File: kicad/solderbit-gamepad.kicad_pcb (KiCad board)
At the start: 2 copper layers, 114 x 49.3 mm, 46 parts, among them J1 Microbit_Edge_Connector, J2 S2B-PH-SM4-TB(LF)(SN), Q1 DMG2045U, SW1 MST22D18G2 125, U1 74HC165D,653, U2 NCP114ASN330T1G

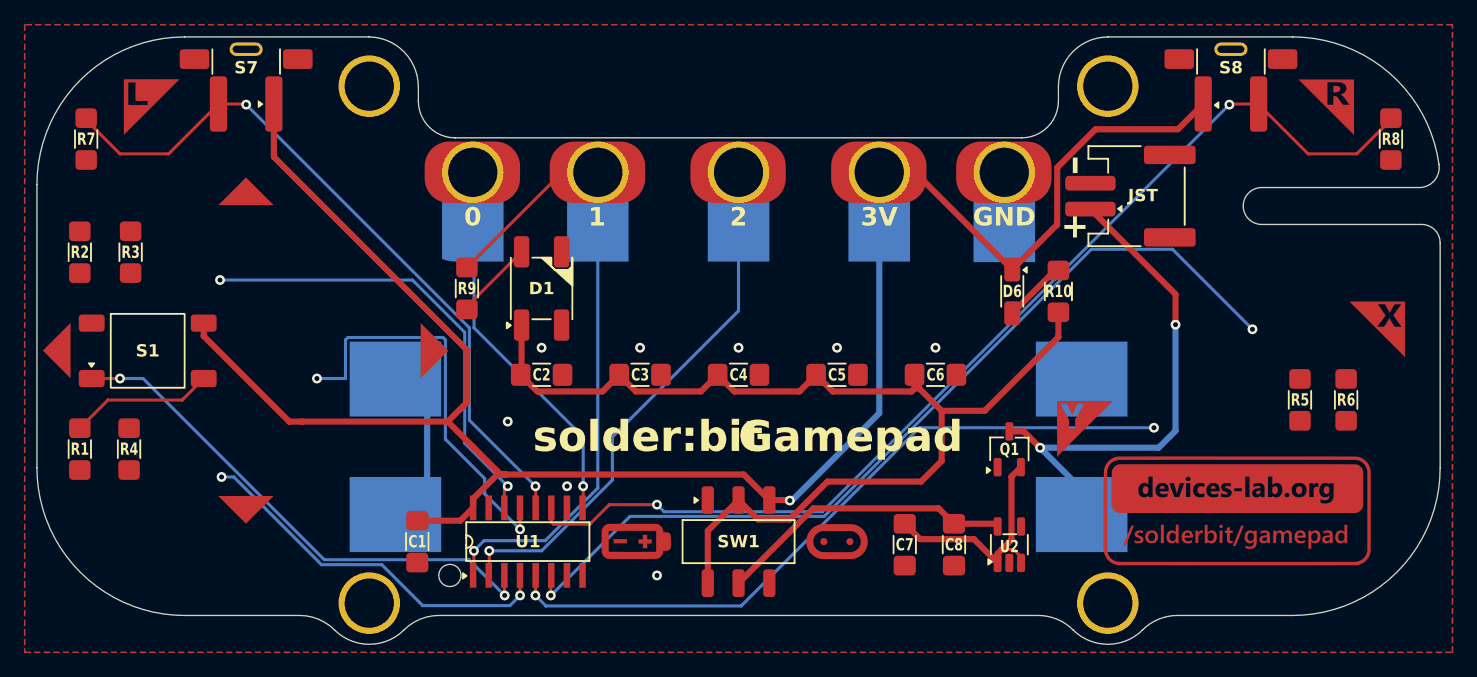
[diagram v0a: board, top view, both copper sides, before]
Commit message: Replace all with v0.9 and new media
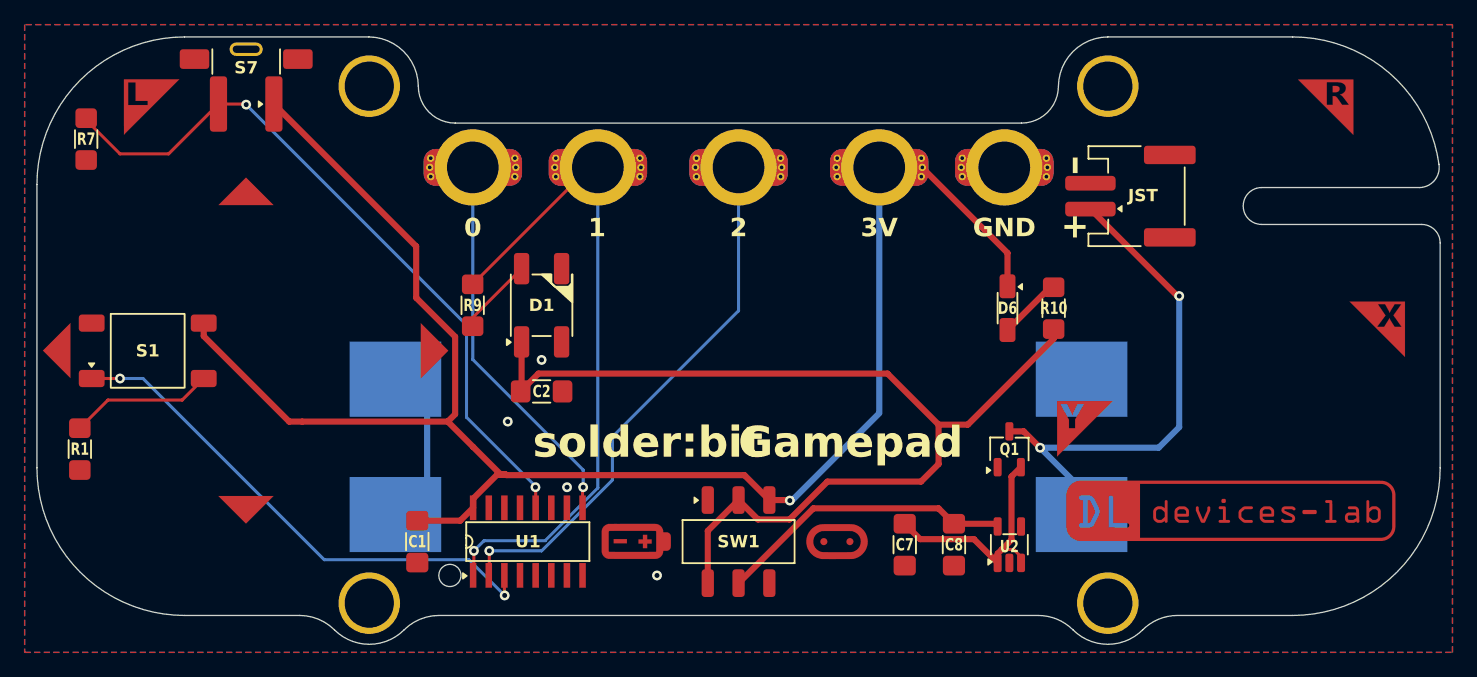
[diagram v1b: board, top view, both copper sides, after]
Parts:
- removed C3, C4, C5, C6: 1uF, Solderbit_Gamepad:1206_Capacitor
- removed G1: ~, Solderbit_Gamepad:Devices-Lab_Logo_H9mm
- removed G4: ~, Solderbit_Gamepad:UKRI_Logo
- removed J1: Microbit_Edge_Connector, Solderbit_Gamepad:Microbit_Edge_Connector
- removed R2, R3, R4, R5, R6, R8: 100k, Solderbit_Gamepad:1206_Resistor
- removed the Ref** at (62.2, 46.6)
- removed S8: TS-1037-A4B3-D2, Solderbit_Gamepad:Tactile_Switch_Right_90_Degrees
- added CN1: SMTSOM310BTR, Solderbit_Gamepad:SMTSOM310BTR, F.Cu at (82.7, 47.2)
- added CN2: SMTSOM310BTR, Solderbit_Gamepad:SMTSOM310BTR, F.Cu at (92.8, 47.2)
- added CN3: SMTSOM310BTR, Solderbit_Gamepad:SMTSOM310BTR, F.Cu at (104.3, 47.2)
- added CN4: SMTSOM310BTR, Solderbit_Gamepad:SMTSOM310BTR, F.Cu at (115.7, 47.2)
- added CN5: SMTSOM310BTR, Solderbit_Gamepad:SMTSOM310BTR, F.Cu at (125.9, 47.2)
- added G***: LOGO, LOGO, F.Cu at (144.3, 75.1)
- added G***: LOGO, LOGO, B.Cu at (147.0, 71.7)
- moved R9 1.44 mm to (82.7, 58.4)
- moved D6 1.42 mm to (126.1, 58.6)
- moved R10 1.42 mm to (129.9, 58.6)
- moved D1 1.36 mm to (88.3, 58.4)
- moved C2 1.35 mm to (88.3, 65.4)
- moved Ref** 0.05 mm to (152.0, 42.3)
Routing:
- net BTN_R_BUMP: track 87.0 -> 0.00 mm, vias 2 -> 0
- net BTN_X: track 73.0 -> 0.00 mm, vias 2 -> 0
- net BTN_Y: track 58.2 -> 0.00 mm, vias 2 -> 0
- net BTN_UP: track 37.5 -> 0.00 mm, vias 2 -> 0
- net BTN_RIGHT: track 33.4 -> 0.00 mm, vias 2 -> 0
- net BTN_DOWN: track 30.6 -> 0.00 mm, vias 2 -> 0
- net Vubit: track 164.0 -> 141.7 mm
- net Vneo: track 89.5 -> 83.1 mm
- net PL/DATA: track 53.7 -> 54.4 mm
- net GND: vias 8 -> 4
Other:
- outline, holes or cut-outs redrawn
- board text added: "${REVISION}"
- board text added: "0"
- board text added: "1"
- board text added: "2"
- board text added: "3V"
- board text added: "GND"
- board text added: "placeholder (delete me)"
- board text removed: "After completing the schamatic, you need to update the PCB. Go to {dblquote}Tools{dblquote} > {dblquote}Update PCB from Schematic...{dblquote} (or press F8). Follow the dialogue, and all components will appear in the corner with {dblquote}ratsnet{dblquote}. Reposition the compoenents, and route them according to the ratsnet."
- board text removed: "H change layer view Alt+3 3D preview R rotate item Shift+M move item X add tracks B fill zones CTRL+B unfill zones"
- board text removed: "Useful keyboard shortcuts"
- board text removed: "Your task"
- board text removed: "v0.7"

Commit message: Cleanup, and add new images
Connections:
- net BTN_DOWN renamed /BTN_DOWN
- net BTN_LEFT renamed /BTN_LEFT
- net BTN_L_BUMP renamed /BTN_L_BUMP
- net BTN_RIGHT renamed /BTN_RIGHT
- net BTN_R_BUMP renamed /BTN_R_BUMP
- net BTN_UP renamed /BTN_UP
- net BTN_X renamed /BTN_X
- net BTN_Y renamed /BTN_Y
- net CLK renamed /CLK
- net PL/DATA renamed /PL/DATA
- net SER renamed /SER
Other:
- board text added: "placeholder"
- board text removed: "placeholder (delete me)"
